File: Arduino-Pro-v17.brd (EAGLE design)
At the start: 100 x 80 mm, 40 parts, among them IC1 ATMEGA1281-16AU, IC2 MCP170312MB, J1 FTDI Basic Programmer

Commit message: BC macz sukz
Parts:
- removed PWM1: (no value), SparkFun-Connectors:1X04
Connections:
- removed net N$12: PWM1.3
- removed net N$13: PWM1.4
- removed net N$17: PWM2.4
- removed net PWM1C: PWM2.3
- net PWM0A: now also PWM2.3; no longer PWM1.1
- net PWM0B: now also PWM2.4; no longer PWM1.2
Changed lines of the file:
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@@
 <attribute name="PROD_ID" value="CONN-09696" x="13.97" y="57.15" size="1.778" layer="27" rot="R270" display="off"/>
-</element>
-<element name="PWM1" library="SparkFun-Connectors" package="1X04" value="" x="13.97" y="16.51" rot="R90">
-<attribute name="PROD_ID" value="CONN-09696" x="13.97" y="16.51" size="1.778" layer="27" rot="R90" display="off"/>
 </element>
 <element name="D1" library="DiscreteComponents" package="DO-214AC" value="" x="43.18" y="58.42" rot="R90"/>
@@
 <wire x1="29.6164" y1="37.9476" x2="29.6037" y2="37.9603" width="0.4064" layer="1"/>
 </signal>
-<signal name="N$12">
-<contactref element="PWM1" pad="3"/>
-</signal>
-<signal name="N$13">
-<contactref element="PWM1" pad="4"/>
-</signal>
-<signal name="PWM1C">
-<contactref element="PWM2" pad="3"/>
-</signal>
-<signal name="N$17">
-<contactref element="PWM2" pad="4"/>
-</signal>
 <signal name="N$21">
 <contactref element="PWM3" pad="4"/>
@@
 <signal name="PWM0B">
 <contactref element="IC1" pad="1"/>
-<contactref element="PWM1" pad="2"/>
 <wire x1="21.4503" y1="51.6255" x2="21.4503" y2="53.4797" width="0.4064" layer="1"/>
 <wire x1="21.4503" y1="53.4797" x2="19.05" y2="55.88" width="0.4064" layer="1"/>
@@
 <wire x1="17.78" y1="55.88" x2="16.51" y2="54.61" width="0.4064" layer="16"/>
 <wire x1="16.51" y1="54.61" x2="16.51" y2="38.1" width="0.4064" layer="16"/>
-<wire x1="16.51" y1="38.1" x2="13.97" y2="19.05" width="0" layer="19" extent="1-16"/>
+<contactref element="PWM2" pad="4"/>
+<wire x1="13.97" y1="26.67" x2="16.51" y2="38.1" width="0" layer="19" extent="16-16"/>
 </signal>
 <signal name="PWM0A">
 <contactref element="IC1" pad="17"/>
-<contactref element="PWM1" pad="1"/>
-<wire x1="13.97" y1="16.51" x2="23.3045" y2="37.9603" width="0" layer="19" extent="1-1"/>
+<contactref element="PWM2" pad="3"/>
+<wire x1="13.97" y1="29.21" x2="23.3045" y2="37.9603" width="0" layer="19" extent="1-1"/>
 </signal>
 <signal name="PWM1B">

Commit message: Almost finished wiring
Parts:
- I2C_PIN: device SparkFun-Connectors:1X05 -> SparkFun-Connectors:1X04
- J2: device SparkFun-Connectors:1X01 -> SparkFun-Connectors:1X02
- moved J2 25.4 mm to (35.6, 62.2), turned to 180 degrees
- moved T1 8.98 mm to (44.5, 53.3)
- moved C13 1.27 mm to (40.6, 39.4)
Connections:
- net 5VROV: now also J2.2
- net GND: no longer I2C_PIN.5
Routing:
- net 3V3: track 23.0 -> 46.1 mm, vias 0 -> 3
- net PWM0A: track 0.00 -> 16.7 mm, vias 0 -> 2
- net PWM0B: track 24.8 -> 39.4 mm
- net PWM1B: track 0.00 -> 13.1 mm, vias 0 -> 1
- net PWM1A: track 0.00 -> 11.6 mm, vias 0 -> 1
- net ALTVCC: track 4.06 -> 15.4 mm, vias 0 -> 2
- net RESET: track 20.7 -> 31.7 mm
- net 5VROV: track 0.00 -> 6.46 mm
- net VCC: track 90.5 -> 84.1 mm, vias 1 -> 3

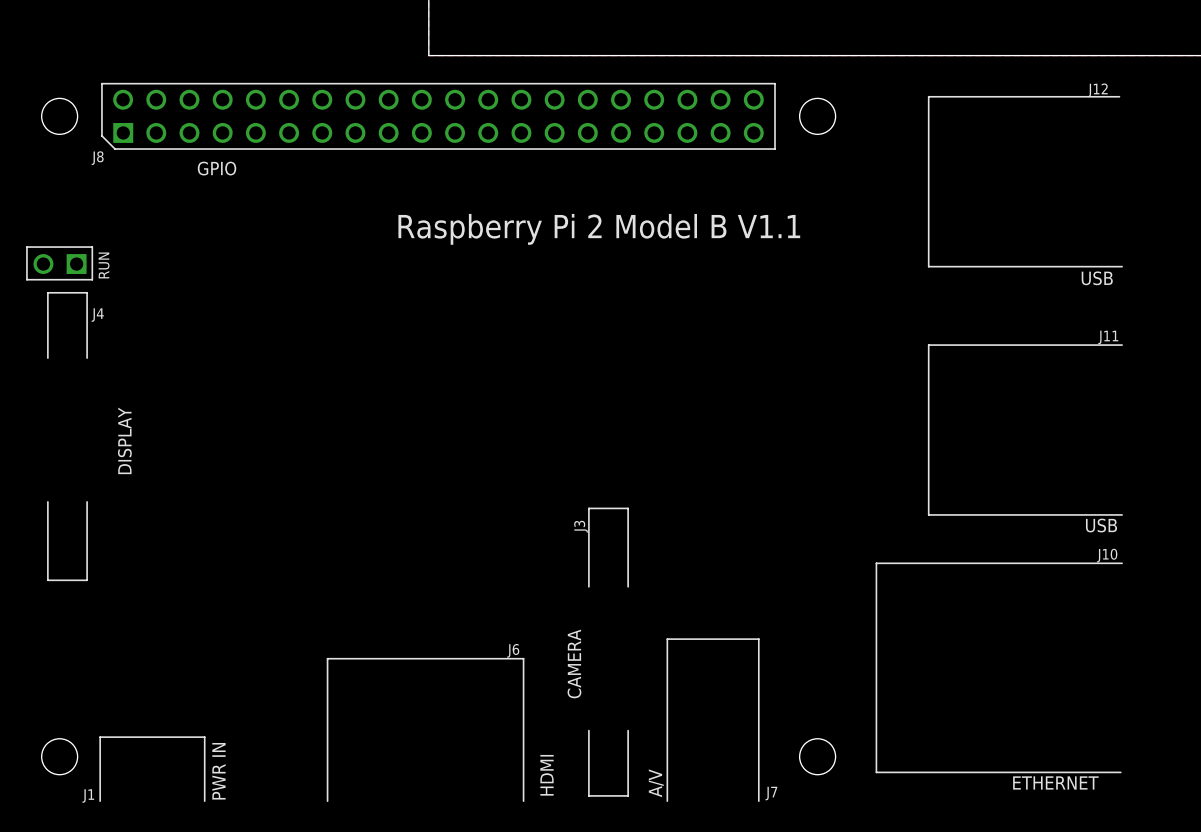
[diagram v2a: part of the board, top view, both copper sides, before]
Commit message: Removed RPI board
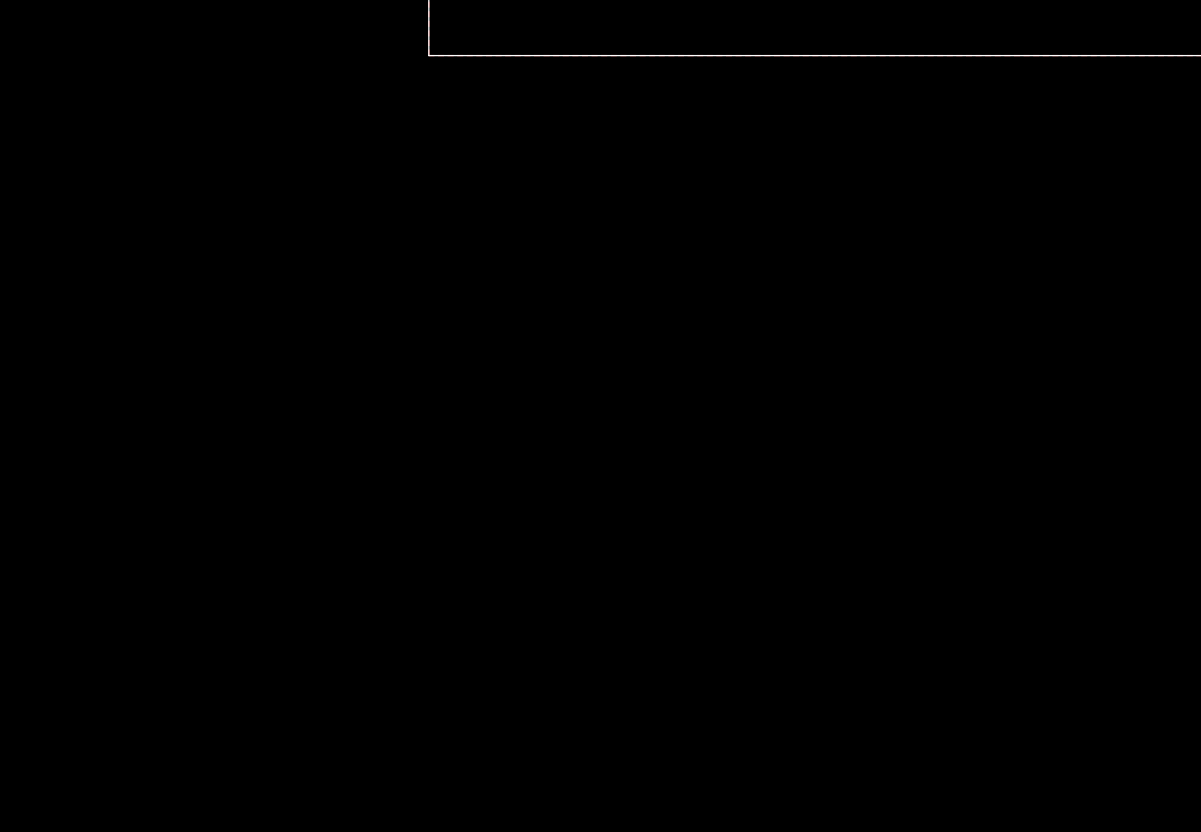
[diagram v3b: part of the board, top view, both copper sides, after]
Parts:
- removed PCB1: RPI2, e14_Rpi2_RevA:RPI2
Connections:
- removed net 3V3CLK: PCB1.P$23
- removed net 3V3MISO: PCB1.P$21
- removed net 3V3MOSI: PCB1.P$19
- net 3V3: no longer PCB1.P$1, PCB1.P$17
- net 5VROV: no longer PCB1.P$2, PCB1.P$4
- net GND: no longer PCB1.P$14, PCB1.P$20, PCB1.P$25, PCB1.P$30, PCB1.P$34, PCB1.P$39, PCB1.P$6, PCB1.P$9
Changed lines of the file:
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@@
 <element name="LED1" library="SparkFun" package="LED-0603" value="Red" x="38.1" y="59.69" rot="R90"/>
 <element name="R11" library="SparkFun" package="0402-RES" value="4.7K" x="38.1" y="58.42" rot="R180"/>
-<element name="PCB1" library="e14_Rpi2_RevA" package="RPI2" value="RPI2" x="-31.75" y="-57.15"/>
 <element name="IC1" library="atmel-2005" package="TQFP64" value="ATMEGA1281-16AU" x="29.21" y="45.72"/>
 <element name="C5" library="SparkFun" package="0402-CAP" value="0.1uF" x="26.67" y="57.15" rot="R270"/>
@@
 <contactref element="R4" pad="1"/>
 <contactref element="R2" pad="1"/>
-<contactref element="PCB1" pad="P$14"/>
-<contactref element="PCB1" pad="P$20"/>
-<contactref element="PCB1" pad="P$30"/>
-<contactref element="PCB1" pad="P$34"/>
-<contactref element="PCB1" pad="P$6"/>
-<contactref element="PCB1" pad="P$25"/>
-<contactref element="PCB1" pad="P$39"/>
-<contactref element="PCB1" pad="P$9"/>
 <contactref element="U$1" pad="1"/>
 <contactref element="J1" pad="6"/>
@@
 </polygon>
 <contactref element="SV1" pad="5"/>
-<wire x1="-13.2334" y1="-5.9182" x2="-18.3134" y2="-3.3782" width="0" layer="19" extent="1-1"/>
-<wire x1="-8.1534" y1="-3.3782" x2="-13.2334" y2="-5.9182" width="0" layer="19" extent="1-1"/>
-<wire x1="-0.5334" y1="-3.3782" x2="-8.1534" y2="-3.3782" width="0" layer="19" extent="1-1"/>
-<wire x1="7.0866" y1="-5.9182" x2="-0.5334" y2="-3.3782" width="0" layer="19" extent="1-1"/>
-<wire x1="12.1666" y1="-3.3782" x2="7.0866" y2="-5.9182" width="0" layer="19" extent="1-1"/>
-<wire x1="17.2466" y1="-3.3782" x2="12.1666" y2="-3.3782" width="0" layer="19" extent="1-1"/>
-<wire x1="24.8666" y1="-5.9182" x2="17.2466" y2="-3.3782" width="0" layer="19" extent="1-1"/>
-<wire x1="27.09" y1="29.21" x2="17.2466" y2="-3.3782" width="0" layer="19" extent="1-1"/>
 <wire x1="38.75" y1="57.15" x2="37.35" y2="59.69" width="0" layer="19" extent="1-1"/>
 <wire x1="41.351" y1="63.271" x2="37.35" y2="59.69" width="0" layer="19" extent="1-1"/>
@@
 </signal>
 <signal name="5VROV">
-<contactref element="PCB1" pad="P$2"/>
-<contactref element="PCB1" pad="P$4"/>
 <contactref element="IC2" pad="2@1"/>
 <contactref element="J2" pad="2"/>
 <wire x1="33.02" y1="62.23" x2="35.56" y2="64.77" width="0.8128" layer="1"/>
 <wire x1="35.56" y1="64.77" x2="38.43" y2="64.77" width="0.8128" layer="1"/>
-<wire x1="-20.8534" y1="-3.3782" x2="33.02" y2="62.23" width="0" layer="19" extent="1-1"/>
-<wire x1="-23.3934" y1="-3.3782" x2="-20.8534" y2="-3.3782" width="0" layer="19" extent="1-1"/>
 </signal>
 <signal name="N$9">
@@
 </signal>
 <signal name="3V3">
-<contactref element="PCB1" pad="P$1"/>
-<contactref element="PCB1" pad="P$17"/>
 <contactref element="J1" pad="4"/>
 <contactref element="D1" pad="A"/>
@@
 <wire x1="40.64" y1="55.88" x2="40.64" y2="58.42" width="0.4064" layer="1"/>
 <wire x1="40.64" y1="58.42" x2="43.18" y2="60.96" width="0.4064" layer="1"/>
-<wire x1="-3.0734" y1="-5.9182" x2="13.97" y2="67.31" width="0" layer="19" extent="1-1"/>
-<wire x1="-23.38" y1="-5.92" x2="-3.0734" y2="-5.9182" width="0" layer="19" extent="1-1"/>
-</signal>
-<signal name="3V3MOSI">
-<contactref element="PCB1" pad="P$19"/>
-</signal>
-<signal name="3V3MISO">
-<contactref element="PCB1" pad="P$21"/>
-</signal>
-<signal name="3V3CLK">
-<contactref element="PCB1" pad="P$23"/>
 </signal>
 <signal name="JTTDI">

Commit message: Finished routing
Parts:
- moved I2C_PIN 1.27 mm to (39.4, 34.3)
- moved IC2 1.27 mm to (40.6, 64.8)
- moved LED1 1.27 mm to (36.8, 59.7)
- moved J2 1.27 mm to (36.8, 62.2)
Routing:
- net VCC: track 84.1 -> 99.4 mm
- net 3V3: track 46.1 -> 49.3 mm
- net RESET: track 31.7 -> 34.1 mm
- net N$38: track 0.00 -> 2.06 mm
- net ALTVCC: track 15.4 -> 14.1 mm, vias 2 -> 1
- net 5VROV: track 6.46 -> 7.21 mm
- net SDA: track 11.7 -> 12.2 mm
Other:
- board size 100 x 80 mm -> 37.8 x 53.3 mm

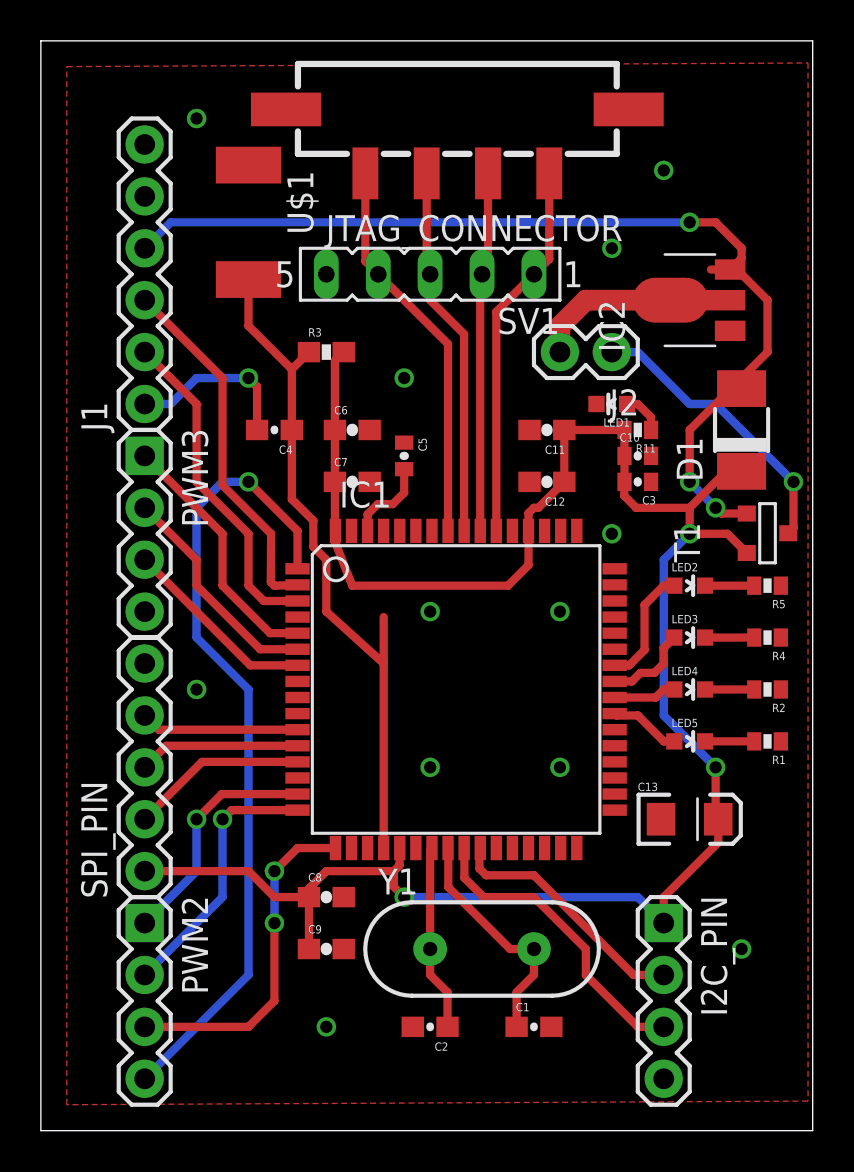
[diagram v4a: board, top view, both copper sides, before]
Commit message: Added ground plan to bottom of board
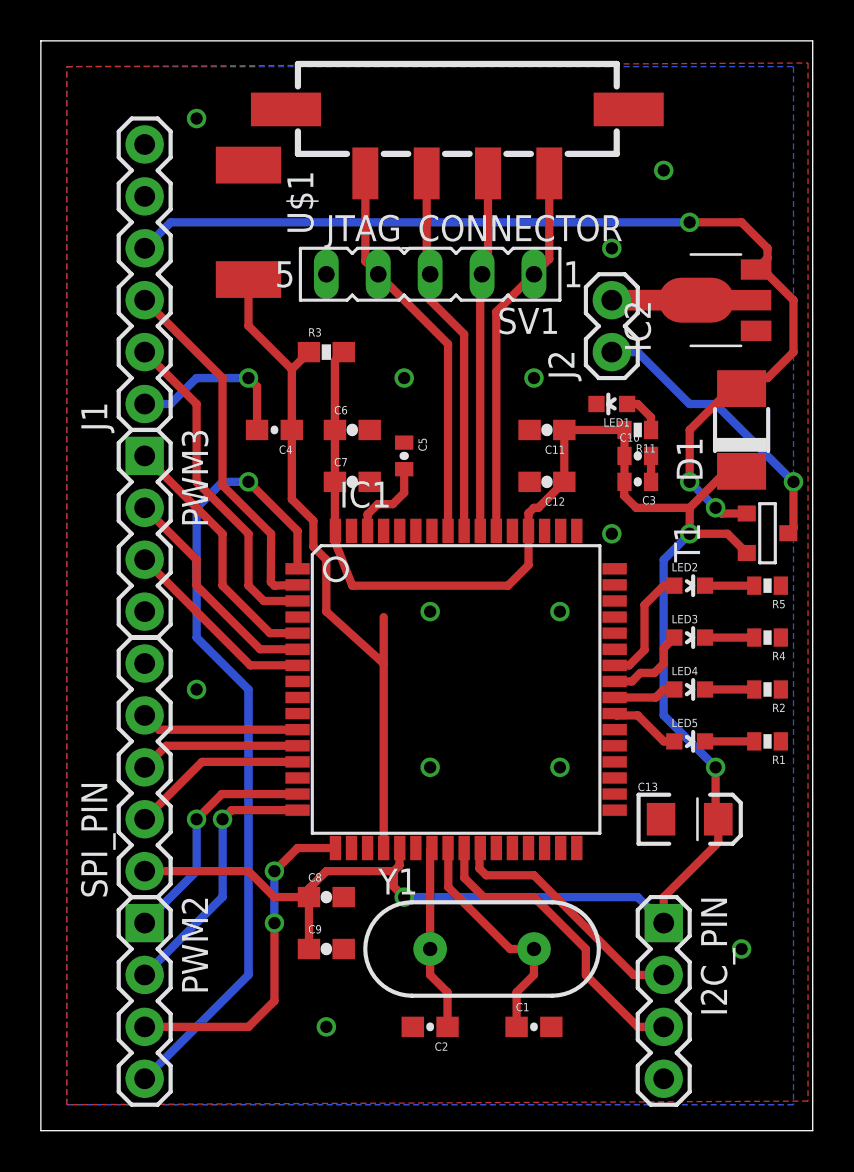
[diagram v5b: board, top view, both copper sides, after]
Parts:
- moved IC2 1.27 mm to (41.9, 64.8)
- turned J2 to 90 degrees
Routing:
- net 5VROV: track 7.21 -> 4.14 mm
- net 3V3: track 49.3 -> 50.9 mm
- net GND: track 0.00 -> 1.27 mm
- added copper zone on layer 16, net GND
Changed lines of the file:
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@@
 <element name="J1" library="SparkFun-Connectors" package="1X06" value="FTDI Basic Programmer" x="13.97" y="59.69" rot="R90"/>
 <element name="C4" library="SparkFun-Capacitors" package="0603-CAP" value="" x="20.32" y="58.42" rot="R180"/>
-<element name="IC2" library="linear" package="SOT89" value="MCP170312MB" x="40.64" y="64.77" rot="R90"/>
-<element name="J2" library="SparkFun-Connectors" package="1X02" value="" x="36.83" y="62.23" rot="R180"/>
+<element name="IC2" library="linear" package="SOT89" value="MCP170312MB" x="41.91" y="64.77" rot="R90"/>
+<element name="J2" library="SparkFun-Connectors" package="1X02" value="" x="36.83" y="62.23" rot="R90"/>
 <element name="C6" library="SparkFun-Passives" package="0603-CAP" value="10uF" x="24.13" y="58.42"/>
 <element name="C7" library="SparkFun-Passives" package="0603-CAP" value="10uF" x="24.13" y="55.88"/>
@@
 <via x="16.51" y="45.72" extent="1-16" drill="0.6" diameter="0.508"/>
 <via x="34.29" y="49.53" extent="1-16" drill="0.6" diameter="0.508"/>
-<via x="36.83" y="53.34" extent="1-16" drill="0.6" diameter="0.508"/>
+<via x="33.02" y="60.96" extent="1-16" drill="0.6" diameter="0.508"/>
 <via x="26.67" y="60.96" extent="1-16" drill="0.6" diameter="0.508"/>
 <via x="36.83" y="67.31" extent="1-16" drill="0.6" diameter="0.508"/>
@@
 <via x="34.29" y="41.91" extent="1-16" drill="0.6" diameter="0.508"/>
 <via x="27.94" y="41.91" extent="1-16" drill="0.6" diameter="0.508"/>
+<wire x1="38.75" y1="55.88" x2="38.75" y2="57.15" width="0.4064" layer="1"/>
+<polygon width="0.4064" layer="16">
+<vertex x="10.16" y="76.2"/>
+<vertex x="45.72" y="76.2"/>
+<vertex x="45.72" y="25.4"/>
+<vertex x="10.16" y="25.4"/>
+</polygon>
 </signal>
 <signal name="RESET">
@@
 <contactref element="C11" pad="1"/>
 <contactref element="C12" pad="1"/>
-<wire x1="37.45" y1="55.88" x2="37.45" y2="57.15" width="0.4064" layer="1"/>
-<wire x1="37.45" y1="57.15" x2="37.45" y2="58.42" width="0.4064" layer="1"/>
-<wire x1="34.505" y1="58.42" x2="37.45" y2="58.42" width="0.4064" layer="1"/>
 <wire x1="34.505" y1="58.42" x2="34.505" y2="55.88" width="0.4064" layer="1"/>
 <wire x1="43.18" y1="56.395" x2="42.425" y2="56.395" width="0.4064" layer="1"/>
@@
 <wire x1="40.64" y1="54.61" x2="38.0238" y2="54.61" width="0.4064" layer="1"/>
 <wire x1="38.0238" y1="54.61" x2="37.4396" y2="55.1942" width="0.4064" layer="1"/>
-<wire x1="37.4396" y1="55.1942" x2="37.4396" y2="55.8696" width="0.4064" layer="1"/>
 <wire x1="37.4396" y1="55.8696" x2="37.45" y2="55.88" width="0.4064" layer="1"/>
 <wire x1="23.28" y1="55.88" x2="23.28" y2="53.5042" width="0.4064" layer="1"/>
@@
 <wire x1="31.75" y1="50.8" x2="24.13" y2="50.8" width="0.4064" layer="1"/>
 <wire x1="23.3045" y1="52.8955" x2="24.13" y2="50.8" width="0.4064" layer="1"/>
+<wire x1="37.4396" y1="55.1942" x2="37.4396" y2="55.8696" width="0.4064" layer="1"/>
+<wire x1="37.45" y1="55.88" x2="37.45" y2="57.15" width="0.4064" layer="1"/>
+<wire x1="37.45" y1="57.15" x2="37.45" y2="58.42" width="0.4064" layer="1"/>
+<wire x1="34.505" y1="58.42" x2="37.45" y2="58.42" width="0.4064" layer="1"/>
 </signal>
 <signal name="N$7">
@@
 <contactref element="IC2" pad="2@1"/>
 <contactref element="J2" pad="2"/>
-<wire x1="34.29" y1="62.23" x2="34.29" y2="63.5" width="1.016" layer="1"/>
-<wire x1="34.29" y1="63.5" x2="35.56" y2="64.77" width="1.016" layer="1"/>
-<wire x1="35.56" y1="64.77" x2="39.37" y2="64.77" width="1.016" layer="1"/>
-<wire x1="39.37" y1="64.77" x2="39.7" y2="64.77" width="0.4064" layer="1"/>
+<wire x1="40.97" y1="64.77" x2="36.83" y2="64.77" width="1.016" layer="1"/>
 </signal>
 <signal name="N$9">
@@
 <contactref element="T1" pad="3"/>
 <contactref element="IC2" pad="3"/>
-<wire x1="42.621" y1="66.269" x2="41.681" y2="66.269" width="0.4064" layer="1"/>
 <wire x1="43.18" y1="60.96" x2="43.18" y2="60.445" width="0.4064" layer="1"/>
 <via x="40.64" y="68.58" extent="1-16" drill="0.6" diameter="0.508"/>
@@
 <wire x1="40.64" y1="55.88" x2="40.64" y2="58.42" width="0.4064" layer="1"/>
 <wire x1="40.64" y1="58.42" x2="43.18" y2="60.96" width="0.4064" layer="1"/>
-<wire x1="40.64" y1="68.58" x2="41.91" y2="68.58" width="0.4064" layer="1"/>
-<wire x1="41.91" y1="68.58" x2="43.18" y2="67.31" width="0.4064" layer="1"/>
-<wire x1="43.18" y1="67.31" x2="43.18" y2="66.828" width="0.4064" layer="1"/>
-<wire x1="43.18" y1="66.828" x2="42.621" y2="66.269" width="0.4064" layer="1"/>
-<wire x1="43.18" y1="60.96" x2="44.45" y2="62.23" width="0.4064" layer="1"/>
-<wire x1="44.45" y1="62.23" x2="44.45" y2="64.77" width="0.4064" layer="1"/>
-<wire x1="44.45" y1="64.77" x2="43.18" y2="66.04" width="0.4064" layer="1"/>
-<wire x1="43.18" y1="66.04" x2="42.85" y2="66.04" width="0.4064" layer="1"/>
-<wire x1="42.85" y1="66.04" x2="42.621" y2="66.269" width="0.4064" layer="1"/>
+<wire x1="40.64" y1="68.58" x2="43.18" y2="68.58" width="0.4064" layer="1"/>
+<wire x1="43.18" y1="68.58" x2="44.45" y2="67.31" width="0.4064" layer="1"/>
+<wire x1="44.45" y1="67.31" x2="44.45" y2="66.828" width="0.4064" layer="1"/>
+<wire x1="44.45" y1="66.828" x2="43.891" y2="66.269" width="0.4064" layer="1"/>
+<wire x1="43.18" y1="60.96" x2="44.45" y2="60.96" width="0.4064" layer="1"/>
+<wire x1="44.45" y1="60.96" x2="45.72" y2="62.23" width="0.4064" layer="1"/>
+<wire x1="45.72" y1="62.23" x2="45.72" y2="64.77" width="0.4064" layer="1"/>
+<wire x1="45.72" y1="64.77" x2="44.45" y2="66.04" width="0.4064" layer="1"/>
+<wire x1="44.45" y1="66.04" x2="44.12" y2="66.04" width="0.4064" layer="1"/>
+<wire x1="44.12" y1="66.04" x2="43.891" y2="66.269" width="0.4064" layer="1"/>
 </signal>
 <signal name="JTTDI">
@@
 <wire x1="36.83" y1="62.23" x2="38.1" y2="62.23" width="0.4064" layer="16"/>
 </signal>
+<signal name="N$2">
+<via x="36.83" y="53.34" extent="1-16" drill="0.6" diameter="0.508"/>
+</signal>
 </signals>
